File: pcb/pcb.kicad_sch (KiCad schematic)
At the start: 9 parts, among them Q1 PNP, SW1 SW_Push, U1 ESP32-WROOM-32, U2 SCD41-D-R2, U3 BME680, U4 1602A_LCD_I2C

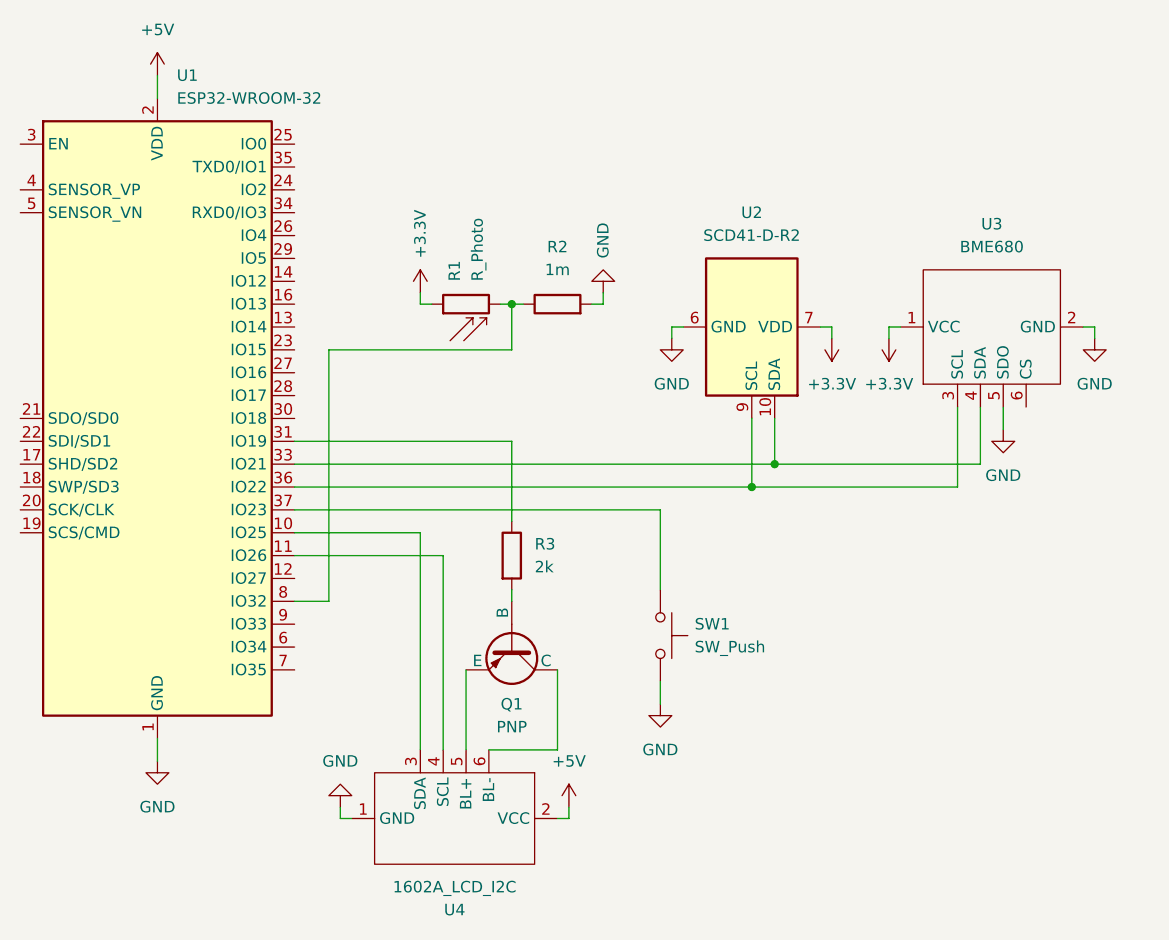
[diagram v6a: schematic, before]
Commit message: working backlight dimming
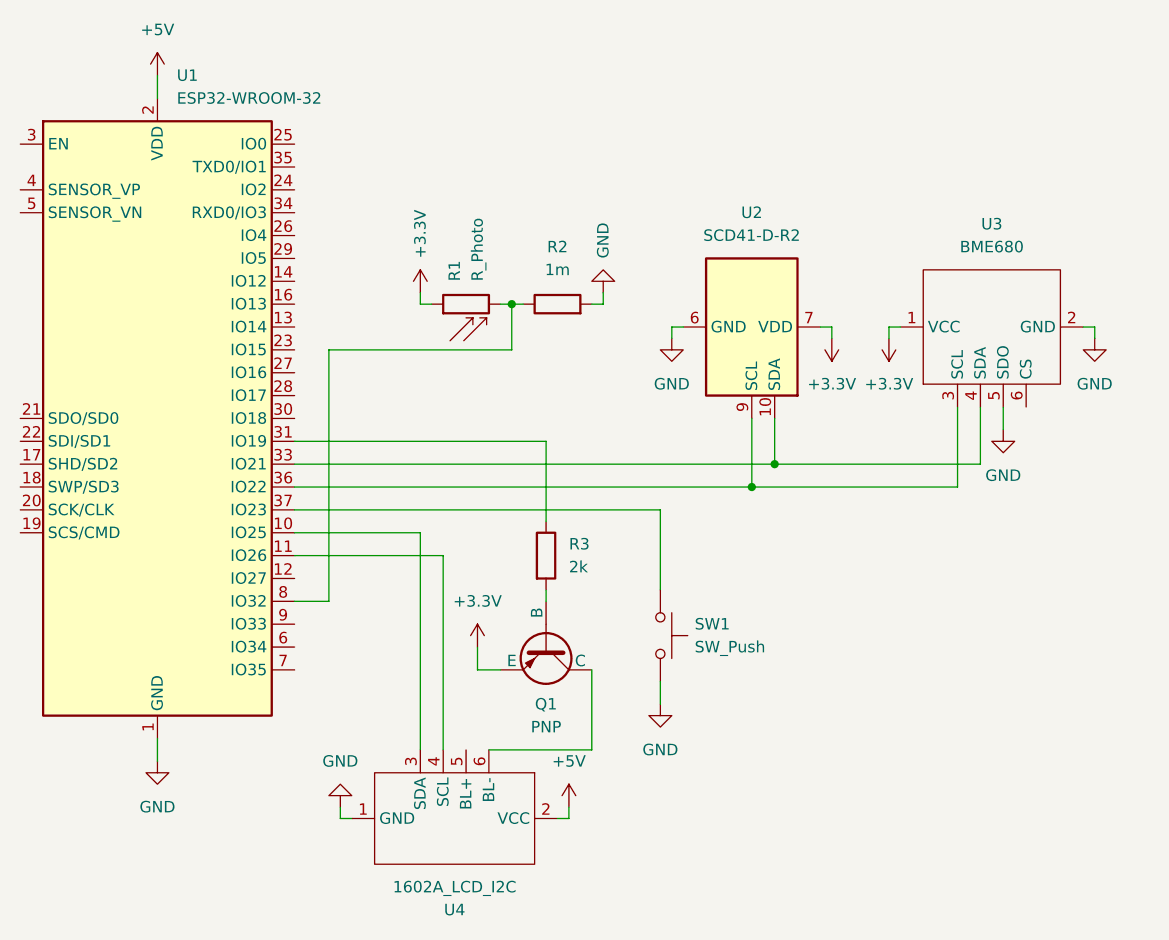
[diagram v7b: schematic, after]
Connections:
- net +3.3V: now also Q1.3 (E)
- net at U4.5 (BL+): no longer Q1.3 (E)
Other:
- moved on the sheet: Q1, R3
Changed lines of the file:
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@@
 	(wire
 		(pts
-			(xy 127 101.6) (xy 151.13 101.6)
+			(xy 127 101.6) (xy 154.94 101.6)
+		)
+		(stroke
+			(width 0)
+			(type default)
+		)
+	)
+	(wire
+		(pts
+			(xy 147.32 127) (xy 149.86 127)
 		)
 		(stroke
@@
 	(wire
 		(pts
-			(xy 148.59 135.89) (xy 156.21 135.89)
+			(xy 148.59 135.89) (xy 160.02 135.89)
 		)
 		(stroke
@@
 	(wire
 		(pts
+			(xy 147.32 124.46) (xy 147.32 127)
+		)
+		(stroke
+			(width 0)
+			(type default)
+		)
+	)
+	(wire
+		(pts
 			(xy 186.69 88.9) (xy 185.42 88.9)
 		)
@@
 	(wire
 		(pts
-			(xy 156.21 135.89) (xy 156.21 127)
+			(xy 160.02 135.89) (xy 160.02 127)
 		)
 		(stroke
@@
 	(wire
 		(pts
-			(xy 151.13 119.38) (xy 151.13 118.11)
+			(xy 154.94 119.38) (xy 154.94 118.11)
 		)
 		(stroke
@@
 	(wire
 		(pts
-			(xy 146.05 127) (xy 146.05 135.89)
-		)
-		(stroke
-			(width 0)
-			(type default)
-		)
-	)
-	(wire
-		(pts
-			(xy 151.13 101.6) (xy 151.13 110.49)
+			(xy 154.94 101.6) (xy 154.94 110.49)
 		)
 		(stroke
@@
 	)
 	(symbol
+		(lib_id "power:+3.3V")
+		(at 147.32 124.46 0)
+		(unit 1)
+		(exclude_from_sim no)
+		(in_bom yes)
+		(on_board yes)
+		(dnp no)
+		(fields_autoplaced yes)
+		(property "Reference" "#PWR013"
+			(at 147.32 128.27 0)
+			(effects
+				(font
+					(size 1.27 1.27)
+				)
+				(hide yes)
+			)
+		)
+		(property "Value" "+3.3V"
+			(at 147.32 119.38 0)
+			(effects
+				(font
+					(size 1.27 1.27)
+				)
+			)
+		)
+		(property "Footprint" ""
+			(at 147.32 124.46 0)
+			(effects
+				(font
+					(size 1.27 1.27)
+				)
+				(hide yes)
+			)
+		)
+		(property "Datasheet" ""
+			(at 147.32 124.46 0)
+			(effects
+				(font
+					(size 1.27 1.27)
+				)
+				(hide yes)
+			)
+		)
+		(property "Description" "Power symbol creates a global label with name \"+3.3V\""
+			(at 147.32 124.46 0)
+			(effects
+				(font
+					(size 1.27 1.27)
+				)
+				(hide yes)
+			)
+		)
+		(pin "1"
+		)
+		(instances
+			(project ""
+				(path "/f8392987-3ddd-437f-94e8-8fae610849f1"
+					(reference "#PWR013")
+					(unit 1)
+				)
+			)
+		)
+	)
+	(symbol
 		(lib_id "Device:R")
 		(at 156.21 86.36 90)
@@
 	(symbol
 		(lib_id "Device:R")
-		(at 151.13 114.3 0)
+		(at 154.94 114.3 0)
 		(unit 1)
 		(exclude_from_sim no)
@@
 		(fields_autoplaced yes)
 		(property "Reference" "R3"
-			(at 153.67 113.0299 0)
+			(at 157.48 113.0299 0)
 			(effects
 				(font
@@
 		)
 		(property "Value" "2k"
-			(at 153.67 115.5699 0)
+			(at 157.48 115.5699 0)
 			(effects
 				(font
@@
 		)
 		(property "Footprint" ""
-			(at 149.352 114.3 90)
+			(at 153.162 114.3 90)
 			(effects
 				(font
@@
 		)
 		(property "Datasheet" "~"
-			(at 151.13 114.3 0)
+			(at 154.94 114.3 0)
 			(effects
 				(font
@@
 		)
 		(property "Description" "Resistor"
-			(at 151.13 114.3 0)
+			(at 154.94 114.3 0)
 			(effects
 				(font
@@
 	(symbol
 		(lib_id "Simulation_SPICE:PNP")
-		(at 151.13 124.46 270)
+		(at 154.94 124.46 270)
 		(unit 1)
 		(exclude_from_sim no)
@@
 		(fields_autoplaced yes)
 		(property "Reference" "Q1"
-			(at 151.13 130.81 90)
+			(at 154.94 130.81 90)
 			(effects
 				(font
@@
 		)
 		(property "Value" "PNP"
-			(at 151.13 133.35 90)
+			(at 154.94 133.35 90)
 			(effects
 				(font
@@
 		)
 		(property "Footprint" ""
-			(at 151.13 160.02 0)
+			(at 154.94 160.02 0)
 			(effects
 				(font
@@
 		)
 		(property "Datasheet" "https://ngspice.sourceforge.io/docs/ngspice-html-manual/manual.xhtml#cha_BJTs"
-			(at 151.13 160.02 0)
+			(at 154.94 160.02 0)
 			(effects
 				(font
@@
 		)
 		(property "Description" "Bipolar transistor symbol for simulation only, substrate tied to the emitter"
-			(at 151.13 124.46 0)
+			(at 154.94 124.46 0)
 			(effects
 				(font
@@
 		)
 		(property "Sim.Device" "PNP"
-			(at 151.13 124.46 0)
+			(at 154.94 124.46 0)
 			(effects
 				(font
@@
 		)
 		(property "Sim.Type" "GUMMELPOON"
-			(at 151.13 124.46 0)
+			(at 154.94 124.46 0)
 			(effects
 				(font
@@
 		)
 		(property "Sim.Pins" "1=C 2=B 3=E"
-			(at 151.13 124.46 0)
-			(effects
-				(font
+			(at 154.94 124.46 0)
+			(effects
+				(font

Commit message: start pcb setup
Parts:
- Q1: footprint (none) -> Package_TO_SOT_THT:TO-3P-3_Vertical
- R1, R2, R3: footprint (none) -> Resistor_THT:R_Axial_DIN0204_L3.6mm_D1.6mm_P1.90mm_Vertical
- SW1: footprint (none) -> Button_Switch_THT:SW_PUSH_6mm
- U3: footprint (none) -> Library:BME680
- U4: footprint (none) -> Library:LCD_I2C
